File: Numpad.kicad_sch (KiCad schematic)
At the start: 105 parts, among them J1 USB_C_Receptacle_USB2.0, J3 AVR-ISP-6, Q2 DMN2041L, SW10 SW_Push, SW11 SW_Push, SW12 SW_Push, SW13 SW_Push, SW14 SW_Push, SW15 SW_Push, SW16 SW_Push, SW17 SW_Push, SW18 SW_Push, SW19 SW_Push, SW2 SW_Push, SW21 SW_Push, SW3 SW_Push, SW4 SW_Push, SW5 SW_Push, SW6 SW_Push, SW7 SW_Push, SW8 SW_Push, SW9 SW_Push, U1 ATmega32U2-A, Y1 16MHz

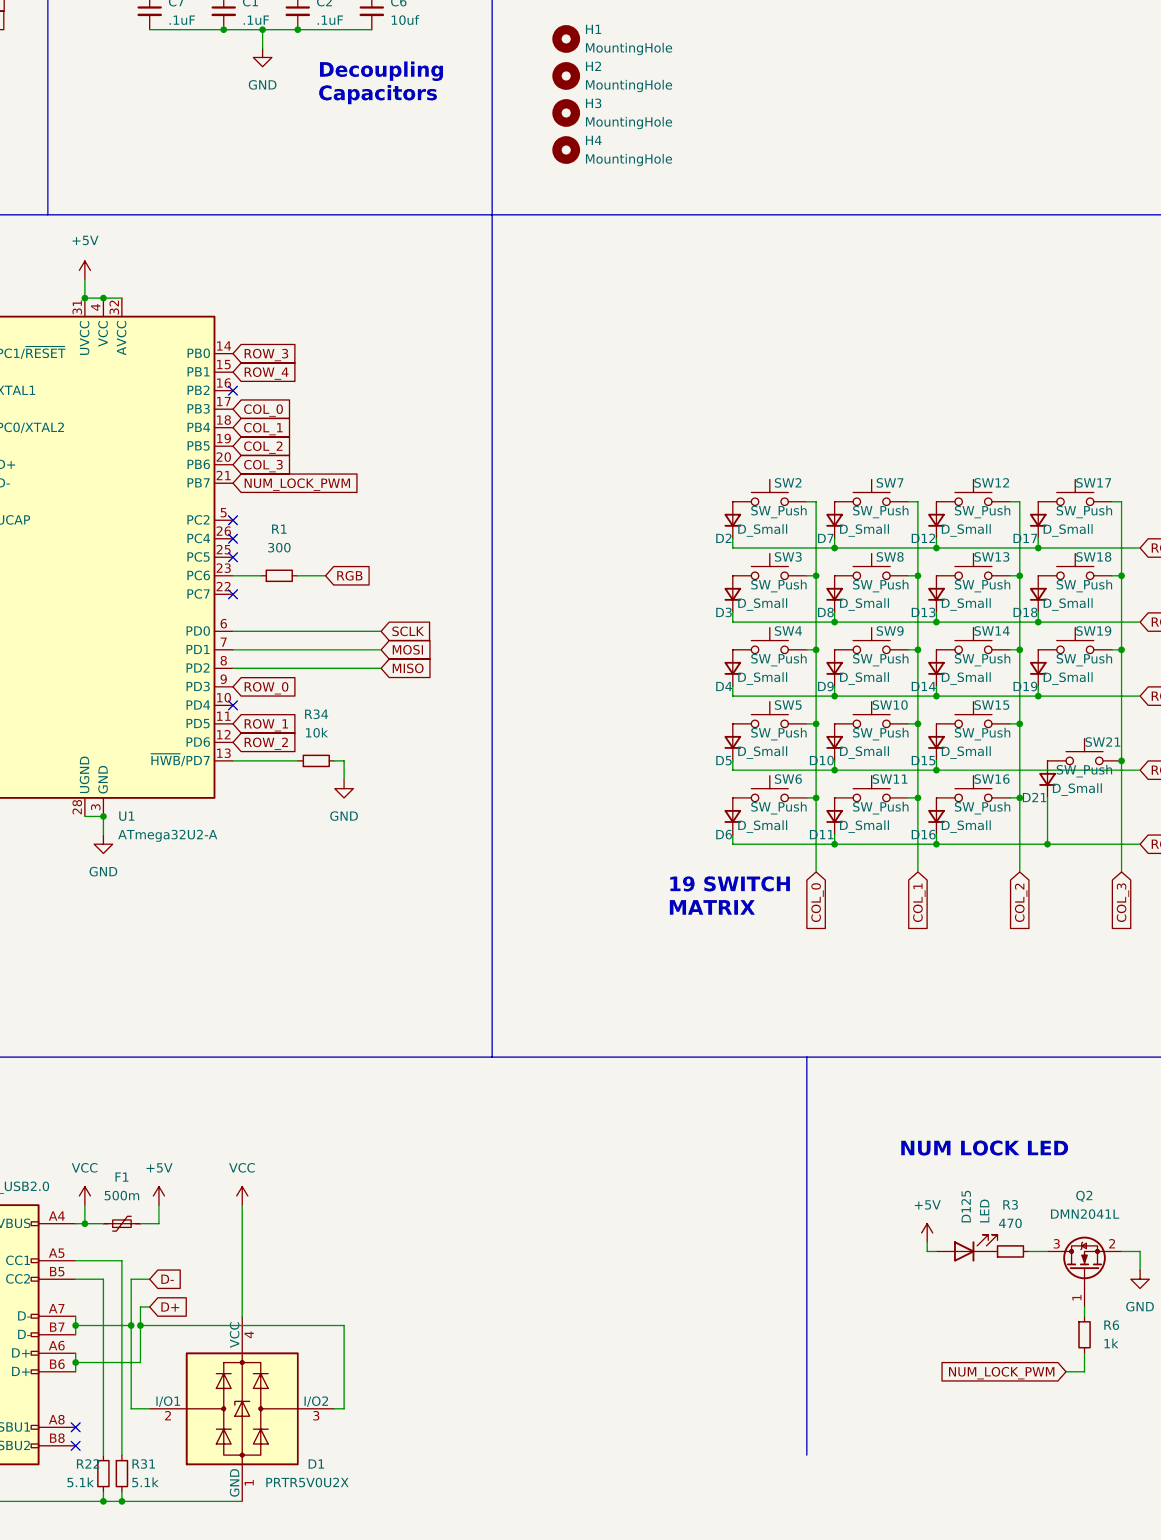
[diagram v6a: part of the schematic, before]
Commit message: redid the numpad quite a bit, including improving the usb and layout
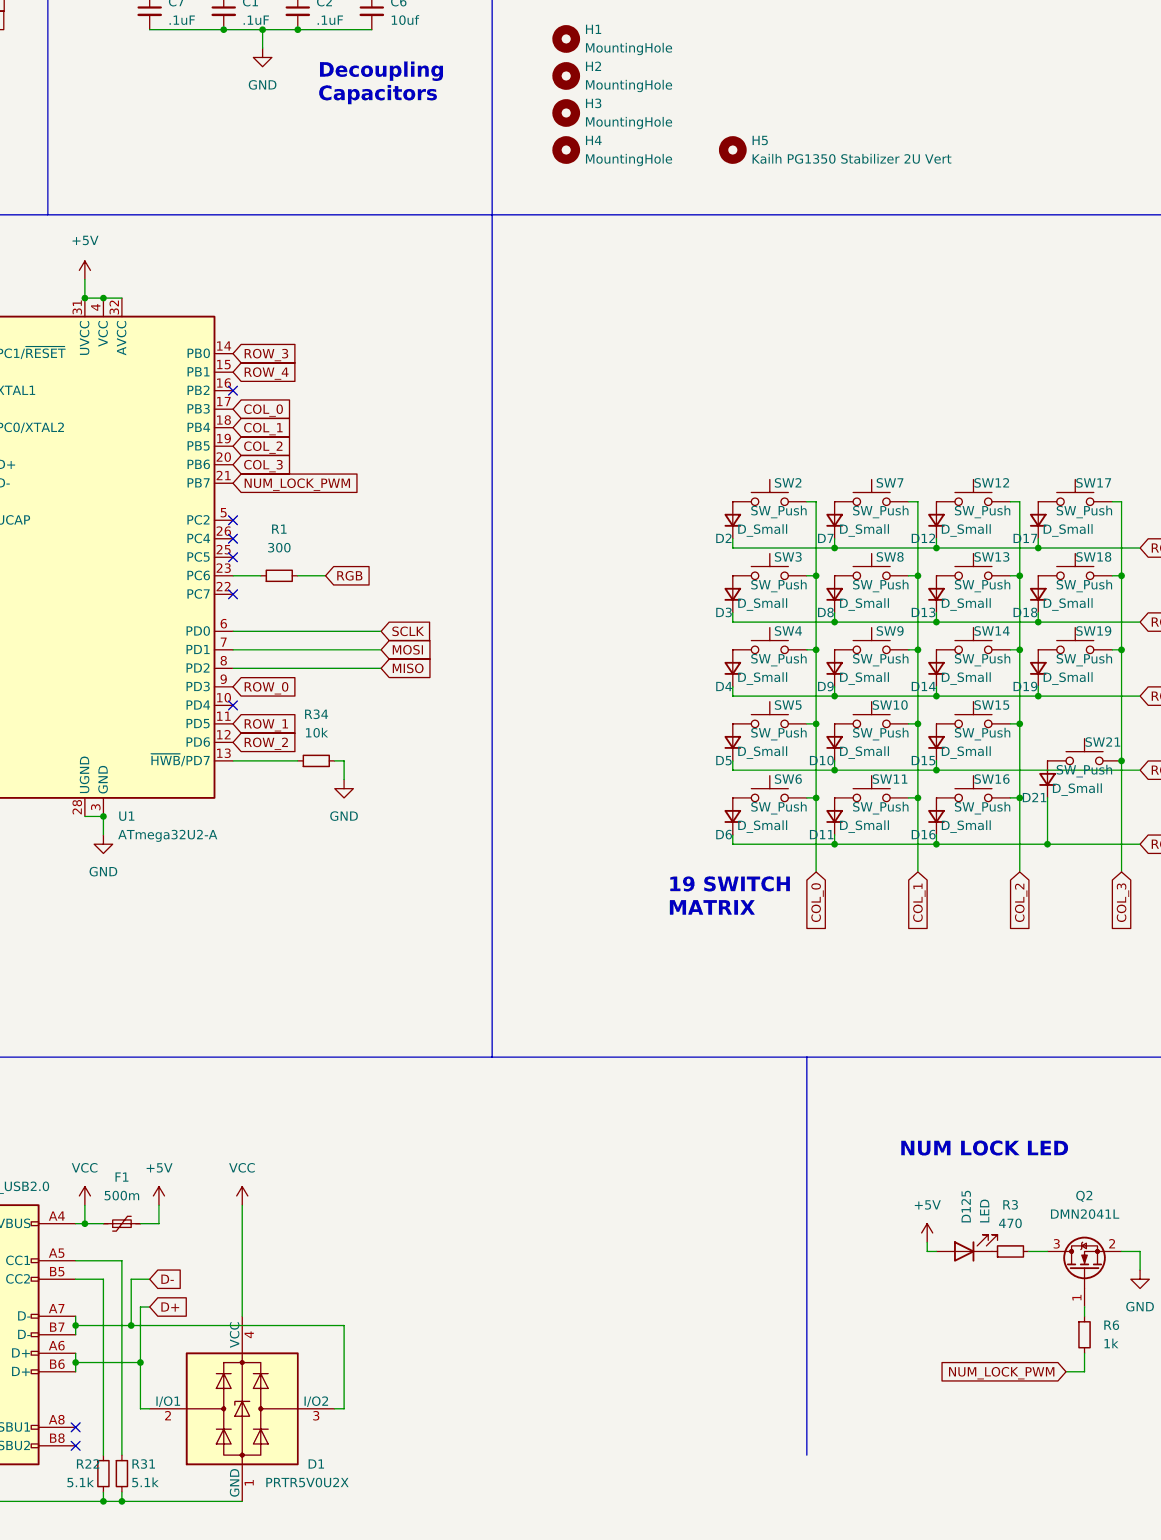
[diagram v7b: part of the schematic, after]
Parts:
- added H5: Kailh PG1350 Stabilizer 2U Vert, Keebio-Parts:Kailh-Stabilizer-2u-Vert, symbol Mechanical:MountingHole
- J1: footprint Connector_USB:USB_C_Receptacle_HRO_TYPE-C-31-M-12 -> Type-C:HRO-TYPE-C-31-M-13
- SW_RESET1: footprint Button_Switch_SMD:SW_SPST_SKQG_WithStem -> Keebio-Parts:SW_SPST_TL3342
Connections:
- net D+: now also D1.2 (I/O1); no longer D1.3 (I/O2)
- net D-: now also D1.3 (I/O2); no longer D1.2 (I/O1)
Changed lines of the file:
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@@
   (junction (at 92.71 87.63) (diameter 0) (color 0 0 0 0)
   )
-  (junction (at 220.98 217.17) (diameter 0) (color 0 0 0 0)
-  )
   (junction (at 72.39 132.08) (diameter 0) (color 0 0 0 0)
   )
@@
   (junction (at 92.71 63.5) (diameter 0) (color 0 0 0 0)
   )
+  (junction (at 220.98 222.25) (diameter 0) (color 0 0 0 0)
+  )
   (junction (at 237.49 34.29) (diameter 0) (color 0 0 0 0)
   )
@@
   (junction (at 313.69 124.46) (diameter 0) (color 0 0 0 0)
   )
+  (junction (at 219.71 217.17) (diameter 0) (color 0 0 0 0)
+  )
   (junction (at 313.69 114.3) (diameter 0) (color 0 0 0 0)
   )
@@
   (junction (at 327.66 114.3) (diameter 0) (color 0 0 0 0)
   )
-  (junction (at 219.71 217.17) (diameter 0) (color 0 0 0 0)
-  )
   (junction (at 341.63 144.78) (diameter 0) (color 0 0 0 0)
   )
@@
     (stroke (width 0) (type default) (color 0 0 0 0))
   )
-  (wire (pts (xy 220.98 217.17) (xy 220.98 222.25))
+  (wire (pts (xy 220.98 214.63) (xy 220.98 222.25))
     (stroke (width 0) (type default) (color 0 0 0 0))
   )
@@
     (stroke (width 0) (type default) (color 0 0 0 0))
   )
-  (wire (pts (xy 248.92 217.17) (xy 220.98 217.17))
-    (stroke (width 0) (type default) (color 0 0 0 0))
-  )
   (wire (pts (xy 72.39 153.67) (xy 72.39 154.94))
     (stroke (width 0) (type default) (color 0 0 0 0))
@@
     (stroke (width 0) (type default) (color 0 0 0 0))
   )
-  (wire (pts (xy 219.71 228.6) (xy 219.71 217.17))
-    (stroke (width 0) (type default) (color 0 0 0 0))
-  )
   (wire (pts (xy 100.33 54.61) (xy 105.41 54.61))
     (stroke (width 0) (type default) (color 0 0 0 0))
@@
     (stroke (width 0) (type default) (color 0 0 0 0))
   )
-  (wire (pts (xy 220.98 214.63) (xy 220.98 217.17))
-    (stroke (width 0) (type default) (color 0 0 0 0))
-  )
   (wire (pts (xy 105.41 63.5) (xy 113.03 63.5))
     (stroke (width 0) (type default) (color 0 0 0 0))
@@
     (stroke (width 0) (type default) (color 0 0 0 0))
   )
+  (wire (pts (xy 219.71 217.17) (xy 248.92 217.17))
+    (stroke (width 0) (type default) (color 0 0 0 0))
+  )
   (wire (pts (xy 92.71 107.95) (xy 92.71 109.22))
     (stroke (width 0) (type default) (color 0 0 0 0))
@@
     (stroke (width 0) (type default) (color 0 0 0 0))
   )
+  (wire (pts (xy 220.98 228.6) (xy 220.98 222.25))
+    (stroke (width 0) (type default) (color 0 0 0 0))
+  )
   (wire (pts (xy 330.2 110.49) (xy 344.17 110.49))
     (stroke (width 0) (type default) (color 0 0 0 0))
@@
     (stroke (width 0) (type default) (color 0 0 0 0))
   )
-  (wire (pts (xy 222.25 228.6) (xy 219.71 228.6))
-    (stroke (width 0) (type default) (color 0 0 0 0))
-  )
   (wire (pts (xy 106.68 68.58) (xy 105.41 68.58))
     (stroke (width 0) (type default) (color 0 0 0 0))
@@
     (stroke (width 0) (type default) (color 0 0 0 0))
   )
+  (wire (pts (xy 222.25 228.6) (xy 220.98 228.6))
+    (stroke (width 0) (type default) (color 0 0 0 0))
+  )
   (wire (pts (xy 193.04 106.68) (xy 193.04 109.22))
     (stroke (width 0) (type default) (color 0 0 0 0))
@@
     (property "Reference" "SW_RESET1" (id 0) (at 187.96 76.2 0))
     (property "Value" "SW_Push" (id 1) (at 187.96 78.74 0))
-    (property "Footprint" "Button_Switch_SMD:SW_SPST_SKQG_WithStem" (id 2) (at 187.96 78.74 0)
+    (property "Footprint" "Keebio-Parts:SW_SPST_TL3342" (id 2) (at 187.96 78.74 0)
       (effects (font (size 1.27 1.27)) hide)
     )
@@
     (property "Reference" "J1" (id 0) (at 196.85 195.58 0))
     (property "Value" "USB_C_Receptacle_USB2.0" (id 1) (at 196.85 198.12 0))
-    (property "Footprint" "Connector_USB:USB_C_Receptacle_HRO_TYPE-C-31-M-12" (id 2) (at 200.66 218.44 0)
+    (property "Footprint" "Type-C:HRO-TYPE-C-31-M-13" (id 2) (at 200.66 218.44 0)
       (effects (font (size 1.27 1.27)) hide)
     )
@@
     (pin "4")
   )
+  (symbol (lib_id "Mechanical:MountingHole") (at 302.26 55.88 0) (unit 1)
+    (in_bom yes) (on_board yes) (fields_autoplaced)
+    (property "Reference" "H5" (id 0) (at 304.8 54.6099 0)
+      (effects (font (size 1.27 1.27)) (justify left))
+    )
+    (property "Value" "Kailh PG1350 Stabilizer 2U Vert" (id 1) (at 304.8 57.1499 0)
+      (effects (font (size 1.27 1.27)) (justify left))
+    )
+    (property "Footprint" "Keebio-Parts:Kailh-Stabilizer-2u-Vert" (id 2) (at 302.26 55.88 0)
+      (effects (font (size 1.27 1.27)) hide)
+    )
+    (property "Datasheet" "~" (id 3) (at 302.26 55.88 0)
+      (effects (font (size 1.27 1.27)) hide)
+    )
+  )
   (symbol (lib_id "Switch:SW_Push") (at 321.31 104.14 0) (unit 1)
     (in_bom yes) (on_board yes) (fields_autoplaced)
@@
       (reference "H4") (unit 1) (value "MountingHole") (footprint "MountingHole:MountingHole_2.2mm_M2_DIN965_Pad")
     )
+    (path "/dc3a5b62-6cc4-4f3e-9c2e-4abf395b2bae"
+      (reference "H5") (unit 1) (value "Kailh PG1350 Stabilizer 2U Vert") (footprint "Keebio-Parts:Kailh-Stabilizer-2u-Vert")
+    )
     (path "/948890ac-a77b-4cab-8a97-45f3b55f1ae8"
-      (reference "J1") (unit 1) (value "USB_C_Receptacle_USB2.0") (footprint "Connector_USB:USB_C_Receptacle_HRO_TYPE-C-31-M-12")
+      (reference "J1") (unit 1) (value "USB_C_Receptacle_USB2.0") (footprint "Type-C:HRO-TYPE-C-31-M-13")
     )
     (path "/e1fbfe0b-9eb9-4b7f-9a02-15c2ac872329"
@@
     )
     (path "/9175ce73-cae1-4cca-a0dd-98fd6e4776f9"
-      (reference "SW_RESET1") (unit 1) (value "SW_Push") (footprint "Button_Switch_SMD:SW_SPST_SKQG_WithStem")
+      (reference "SW_RESET1") (unit 1) (value "SW_Push") (footprint "Keebio-Parts:SW_SPST_TL3342")
     )
     (path "/6fc164d8-33c7-4a71-9d93-4fd96f31af80"
